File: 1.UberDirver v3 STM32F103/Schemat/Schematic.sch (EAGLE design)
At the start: 86 parts, among them U2 STM32F10XTXU6HS

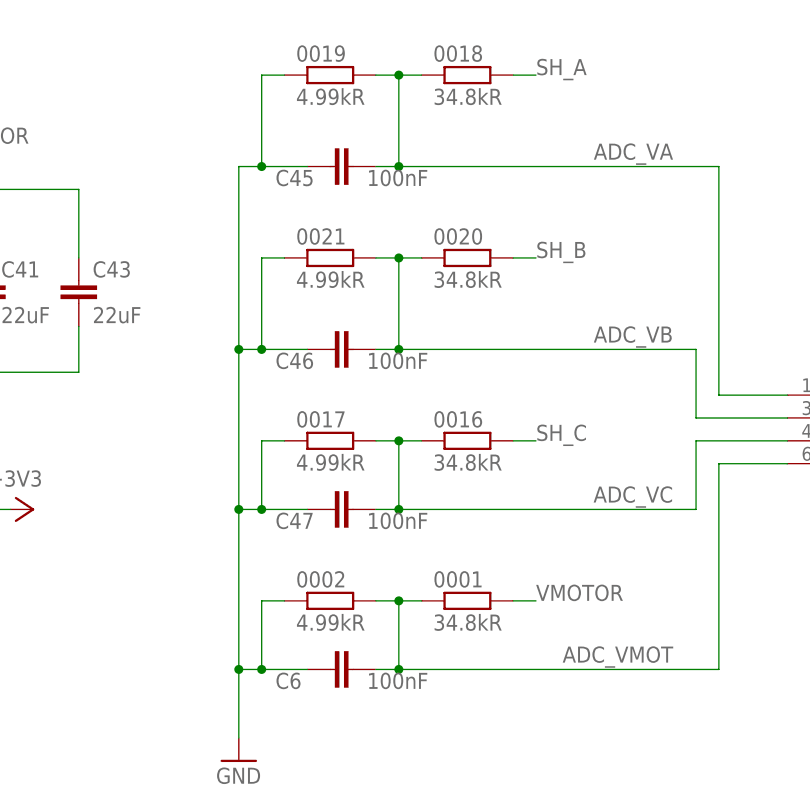
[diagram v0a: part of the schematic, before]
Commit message: Current is stm32f103 V3
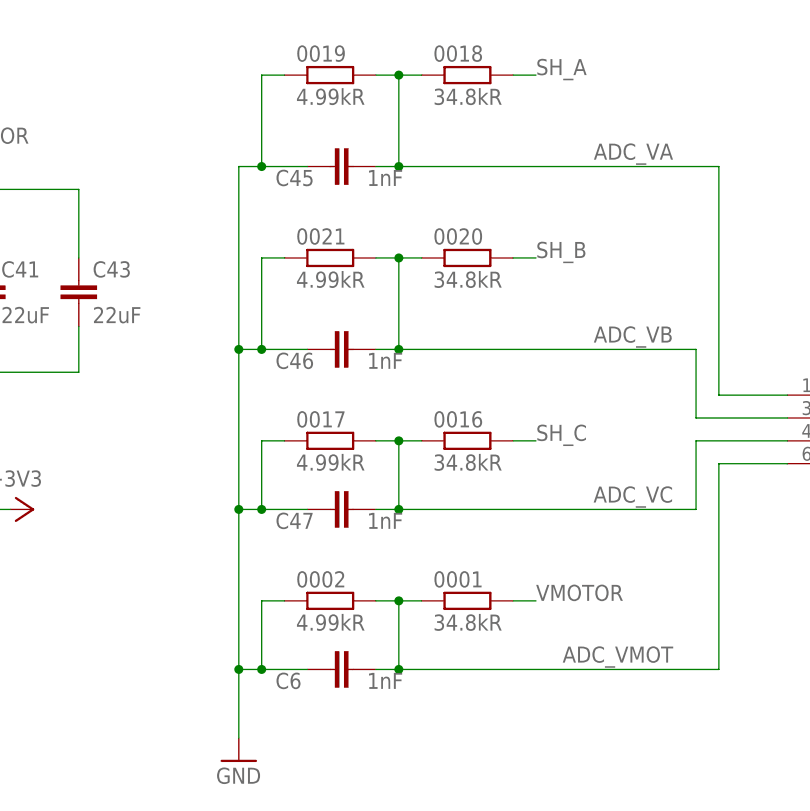
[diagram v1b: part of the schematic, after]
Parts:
- C45, C46, C47, C6: value 100nF -> 1nF
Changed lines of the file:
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@@
 <part name="0020" library="rcl" library_urn="urn:adsk.eagle:library:334" deviceset="R-EU_" device="R0402" package3d_urn="urn:adsk.eagle:package:23547/3" value="34.8kR"/>
 <part name="0021" library="rcl" library_urn="urn:adsk.eagle:library:334" deviceset="R-EU_" device="R0402" package3d_urn="urn:adsk.eagle:package:23547/3" value="4.99kR"/>
-<part name="C45" library="rcl" deviceset="C-EU" device="" package3d_urn="urn:adsk.eagle:package:23547/3" value="100nF"/>
-<part name="C46" library="rcl" deviceset="C-EU" device="" package3d_urn="urn:adsk.eagle:package:23547/3" value="100nF"/>
-<part name="C47" library="rcl" deviceset="C-EU" device="" package3d_urn="urn:adsk.eagle:package:23547/3" value="100nF"/>
+<part name="C45" library="rcl" deviceset="C-EU" device="" package3d_urn="urn:adsk.eagle:package:23547/3" value="1nF"/>
+<part name="C46" library="rcl" deviceset="C-EU" device="" package3d_urn="urn:adsk.eagle:package:23547/3" value="1nF"/>
+<part name="C47" library="rcl" deviceset="C-EU" device="" package3d_urn="urn:adsk.eagle:package:23547/3" value="1nF"/>
 <part name="+3V11" library="supply1" library_urn="urn:adsk.eagle:library:371" deviceset="+3V3" device=""/>
 <part name="U$31" library="tpd4e001" deviceset="TPD4E001" device=""/>
@@
 <part name="0001" library="rcl" library_urn="urn:adsk.eagle:library:334" deviceset="R-EU_" device="R0402" package3d_urn="urn:adsk.eagle:package:23547/3" value="34.8kR"/>
 <part name="0002" library="rcl" library_urn="urn:adsk.eagle:library:334" deviceset="R-EU_" device="R0402" package3d_urn="urn:adsk.eagle:package:23547/3" value="4.99kR"/>
-<part name="C6" library="rcl" deviceset="C-EU" device="" package3d_urn="urn:adsk.eagle:package:23547/3" value="100nF"/>
+<part name="C6" library="rcl" deviceset="C-EU" device="" package3d_urn="urn:adsk.eagle:package:23547/3" value="1nF"/>
 <part name="LED9" library="led" library_urn="urn:adsk.eagle:library:259" deviceset="LED" device="SML0603" package3d_urn="urn:adsk.eagle:package:15832/1" value="Red"/>
 <part name="R24" library="rcl" library_urn="urn:adsk.eagle:library:334" deviceset="R-EU_" device="R0402" package3d_urn="urn:adsk.eagle:package:23547/3" value="10k"/>

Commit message: Inzynier zrobiony
dodano wersje 3
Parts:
- removed 0001, 0016, 0018, 0020: 34.8kR, rcl:R-EU_R0402
- removed 0002, 0017, 0019, 0021: 4.99kR, rcl:R-EU_R0402
- removed 0015: 5mohm, resistor:R-EU_R2512
- removed C49: 100nF, rcl:C-EU
- removed C67, C68, C69: 220uf, rcl:CPOL-EU150CLZ-0810
- added C24\, C25, C26, C27: 22uF/35V, rcl:C-EUC1206
- added C28: 220uf, rcl:CPOL-EU150CLZ-0810
- added C48: (no value), rcl:C-EU025-040X050
- added D2, D3, D4, D5: (no value), adafruit:DIODE_SOD-123FL
- added L1: 1mH, resistor:R-EU_R0603
- added L2, L3, L4: (no value), rcl:L-US0204/5
- added PAD_A1, PAD_A2: (no value), wirepad:SMD5
- added Q10, Q11, Q12, Q13, Q14, Q7, Q8, Q9: CSD17573Q5B, CSD_Mosfet:CSD17573Q5B
- added R10: 10k, rcl:R-EU_R0402
- added R11: 100R, resistor:R-EU_R0603
- added R2, R4, R6, R8: 4.99kR, rcl:R-EU_R0402
- added R21, R22, R23: (no value), rcl:R-EU_0204/5
- added R3, R5, R7: 100k, rcl:R-EU_R0402
- C1, C2, C3: value 100nF -> 1nF
- C10, C11: value 220uf -> 0.047uF; device rcl:CPOL-EU150CLZ-0810 -> rcl:C-EU
- C12: value 220uf -> 4.7uF/50V; device rcl:CPOL-EU150CLZ-0810 -> rcl:C-EUC0805
- C13: value 4.7uF -> 4.7uF/50V
- C14: value 4.7uF -> 1nF; device rcl:C-EUC0805 -> rcl:C-EU
- C15, C4: value 220uf -> 1nF; device rcl:CPOL-EU150CLZ-0810 -> rcl:C-EU
- C16, C18, C20, C22: value 220uf -> 100nF; device rcl:CPOL-EU150CLZ-0810 -> rcl:C-EU
- C17, C19, C21, C23: value 220uf -> 4.7uF; device rcl:CPOL-EU150CLZ-0810 -> rcl:C-EU
- C24: value 220uf -> (none); device rcl:CPOL-EU150CLZ-0810 -> rcl:C-EU025-040X050
- C29, C35, C37, C40: value 4.7uF -> 220uf; device rcl:C-EU -> rcl:CPOL-EU150CLZ-0810
- C30, C33, C41, C43: value 22uF -> 220uf; device rcl:C-EUC1206 -> rcl:CPOL-EU150CLZ-0810
- C31, C32: value 0.047uF -> 220uf; device rcl:C-EU -> rcl:CPOL-EU150CLZ-0810
- C34, C36, C38, C39: value 1uF -> 220uf; device rcl:C-EU -> rcl:CPOL-EU150CLZ-0810
- C42, C44, C45, C46, C47: value 1nF -> 220uf; device rcl:C-EU -> rcl:CPOL-EU150CLZ-0810
- C6: value 1nF -> 1uF
- C7, C8, C9: value 220uf -> 1uF; device rcl:CPOL-EU150CLZ-0810 -> rcl:C-EU
- R1: value 180nH -> 100k; device resistor:R-EU_R0603 -> rcl:R-EU_R0402
- R13: value 100R -> 5mohm; device resistor:R-EU_R0603 -> resistor:R-EU_R2512
- R24: value 10k -> (none); device rcl:R-EU_R0402 -> rcl:R-EU_0204/5
- renumbered 0014 to R12, LED9 to D1, MOTOR_PAD_C to PAD_C, M_A to PAD_A, M_B to PAD_B, R16 to R9, U$22 to Q3, U$23 to Q4, U$24 to Q1, U$25 to Q2, U$26 to Q5, U$28 to Q6
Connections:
- new net +VCC: Q10.D, Q11.D, Q9.D
- new net N$15: PAD_A1.P, R21.2
- new net N$17: C48.1, D2.A, D3.C, R21.1, R22.2
- new net N$18: C48.2, D3.A, R22.1
- new net N$19: PAD_A2.P, R23.2
- new net N$24: D2.C
- new net N$25: C24.1, D4.A, D5.C, R23.1, R24.2
- new net N$26: C24.2, D5.A, R24.1
- new net N$27: D4.C
- new net N$29: Q7.S, Q8.D
- new net N$31: Q8.G
- new net N$32: Q7.G
- new net N$41: L2.1, Q12.D, Q9.S
- new net N$42: L4.1, Q10.S, Q13.D
- new net N$43: L3.1, Q11.S, Q14.D
- new net N$45: L2.2, L3.2, L4.2
- new net VCC: Q7.D
- net +3V3: now also C18.1, C19.1, C20.1, C21.1, C22.1, C23.1, C6.1, L1.2; no longer C1.1, C2.1, C29.1, C35.1, C37.1, C39.1, C49.1, R1.2
- net ADC_VA: now also C4.1, R7.1, R8.2; no longer 0018.1, 0019.2, C45.1
- net ADC_VB: now also C3.1, R5.1, R6.2; no longer 0020.1, 0021.2, C46.1
- net ADC_VC: now also C2.1, R3.1, R4.2; no longer 0016.1, 0017.2, C47.1
- net ADC_VMOT: now also C1.1, R1.1, R2.2; no longer 0001.1, 0002.2, C6.1
- net GND: now also C16.2, C17.2, C18.2, C19.2, C20.2, C21.2, C22.2, C23.2, C24\.2, C25.2, C26.2, C27.2, C28.-, C29.-, C30.-, C31.-, C32.-, C33.-, C34.-, C35.-, C36.-, C37.-, C38.-, C39.-, C4.2, C40.-, C41.-, C42.-, C43.-, C44.-, C45.-, C46.-, C47.-, C7.2, C8.2, C9.2, Q12.S, Q13.S, Q14.S, Q8.S, R10.1, R13.1, R2.1, R4.1, R6.1, R8.1; no longer 0002.1, 0015.1, 0017.1, 0019.1, 0021.1, C10.-, C11.-, C12.-, C15.-, C16.-, C17.-, C18.-, C19.-, C20.-, C21.-, C22.-, C23.-, C24.-, C29.2, C30.2, C33.2, C34.2, C35.2, C36.2, C37.2, C38.2, C39.2, C4.-, C40.2, C41.2, C43.2, C45.2, C46.2, C47.2, C49.2, C67.-, C68.-, C69.-, C7.-, C8.-, C9.-, R24.1
- net GND_A: now also C14.2; no longer C42.2
- net GND_C: now also C15.2; no longer C44.2
- net N$10: now also C9.1; no longer C36.1
- net N$12: now also C8.1; no longer C34.1
- net N$13: now also C7.1; no longer C38.1
- net N$14: now also C11.2; no longer C31.2
- net N$16: now also C11.1; no longer C31.1
- net N$2: now also C16.1, C17.1, L1.1; no longer C3.1, C40.1, R1.1
- net N$20: now also C10.2; no longer C32.2
- net N$21: now also C10.1; no longer C32.1
- net N$22: now also R11.1; no longer R13.1
- net N$23: now also C12.2; no longer C14.2
- net N$81: now also R10.2; no longer R24.2
- net SH_A: now also R7.2; no longer 0018.2
- net SH_B: now also R5.2; no longer 0020.2
- net SH_C: now also R3.2; no longer 0016.2
- net SL_A: now also C14.1; no longer C42.1
- net SL_C: now also C15.1, R13.2; no longer 0015.2, C44.1
- net VMOTOR: now also C12.1, C24\.1, C25.1, C26.1, C27.1, C28.+, C29.+, C30.+, C31.+, C32.+, C33.+, C34.+, C35.+, C36.+, C37.+, C38.+, C39.+, C40.+, C41.+, C42.+, C43.+, C44.+, C45.+, C46.+, C47.+, R1.2, R11.2; no longer 0001.2, C10.+, C11.+, C12.+, C14.1, C15.+, C16.+, C17.+, C18.+, C19.+, C20.+, C21.+, C22.+, C23.+, C24.+, C30.1, C33.1, C4.+, C41.1, C43.1, C67.+, C68.+, C69.+, C7.+, C8.+, C9.+, R13.2
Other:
- note added: "+VDC"
- note added: "1"
- note added: "2"
- note added: "2x I/O"
- note added: "3"
- note added: "3x ADC"
- note added: "6x PWM"
- note added: "CAN"
- note added: "CSD18510Q5B"
- note added: "DRV8305"
- note added: "Faza A"
- note added: "Faza B"
- note added: "Faza C"
- note added: "GND"
- note added: "LED"
- note added: "Napięcie zasilania"
- note added: "PWM"
- note added: "Pomiar prądów i napięć"
- note added: "Pompma ładunku"
- note added: "Półmostek"
- note added: "SILNIK"
- note added: "SPI"
- note added: "Sekcja Mocy"
- note added: "Sekcja sterowania"
- note added: "Sekwencja"
- note added: "Silnik"
- note added: "Stabilizator liniowy"
- note added: "Sterowanie tranzystorami"
- note added: "Sterowanie zewnętrzne"
- note added: "Sterownik"
- note added: "Sterownik bramek"
- note added: "Sygnały sterujące"
- note added: "UART"
- note added: "Urządzenie sterujące"
- moved on the sheet: C1, C13, C14, C2, C3, C5, C6, R1, R13, R24
